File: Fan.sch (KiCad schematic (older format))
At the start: 0 parts

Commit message: Added Powercontrol stuff
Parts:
- added Q?: MOSFET_N, ~, symbol MOSFET_N
- added R? (x5): R, ~, symbol R
- added RV?: POT, ~, symbol POT
- added U?: LM324, symbol LM324
- added U?: MCP4922-E/P, DIP14, symbol MCP4922-E/P
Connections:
- net labels added: +12V, -12V, AGND, CS_N, Current Measure, Fan_in, MISO, MOSI, SCLK, Tach_out
- net labels removed: Fanin, Tachout
- wire segments 0 -> 34

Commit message: Struktur nach Arduino
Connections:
- net labels added: CURR_MEAS, FAN_EN_N, FAN_OUT+, FAN_OUT-, TACH_IN, TACH_MEAS
- net labels removed: Current Measure, Fan_in, Power+, Power-, Tach, Tach_out
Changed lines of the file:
@@
 Sheet 8 9
 Title ""
-Date "4 feb 2014"
+Date "6 feb 2014"
 Rev ""
 Comp ""
@@
 Comment4 ""
 $EndDescr
-Text HLabel 10500 2200 0    60   Input ~ 0
-Power+
-Text HLabel 10500 2400 0    60   Input ~ 0
-Power-
+Text HLabel 10500 2200 0    60   Output ~ 0
+FAN_OUT+
+Text HLabel 10500 2400 0    60   Output ~ 0
+FAN_OUT-
 Text HLabel 10350 2800 0    60   Input ~ 0
-Tach
+TACH_IN
 Text HLabel 1350 3300 0    60   Output ~ 0
-Tach_out
+TACH_MEAS
 Text HLabel 1350 2700 0    60   Input ~ 0
-Fan_in
+FAN_EN_N
 $Comp
 L LM324 U?
@@
 $EndComp
 Text HLabel 1400 2900 0    60   Output ~ 0
-Current Measure
+CURR_MEAS
 $Comp
 L R R?

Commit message: Fan/Current Module Refactoring
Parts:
- removed R? (x3): R, ~, symbol R
- removed RV?: POT, ~, symbol POT
- added D?: DIODE, ~, symbol DIODE
- added Q? (x2): MOSFET_N, ~, symbol MOSFET_N
- added TH?: THERMISTOR, ~, symbol THERMISTOR
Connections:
- net labels added: +12C, FAN_MODE, FAN_PWM_N
- net labels removed: FAN_EN_N
- wire segments 34 -> 36
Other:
- moved on the sheet: Q?, R?, U?, U?A

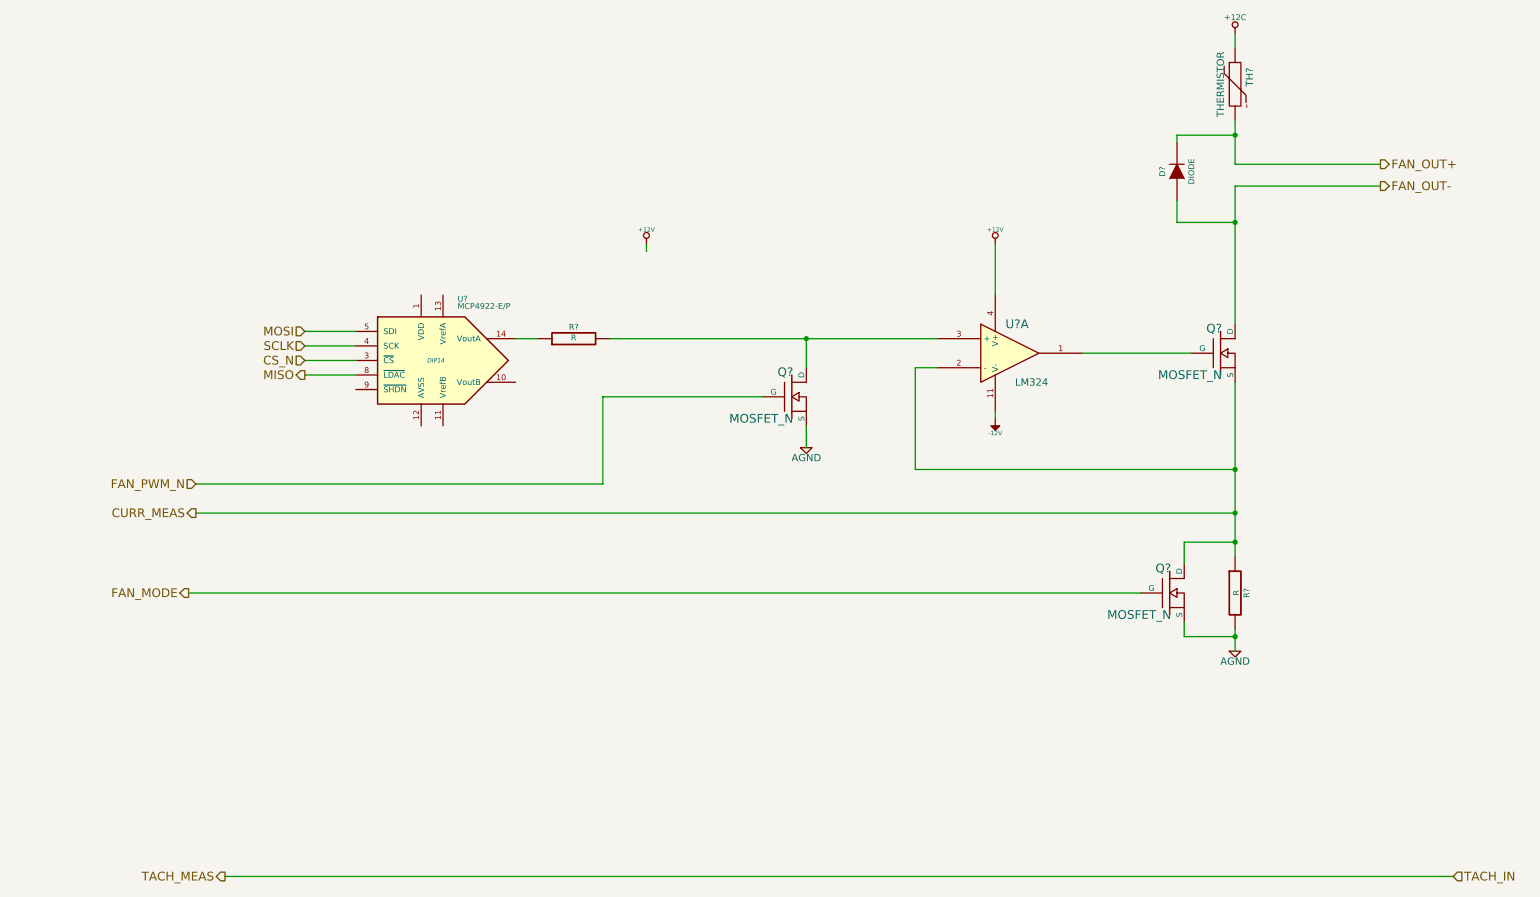
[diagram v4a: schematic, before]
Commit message: Nach Einfuegen Relay-Modul
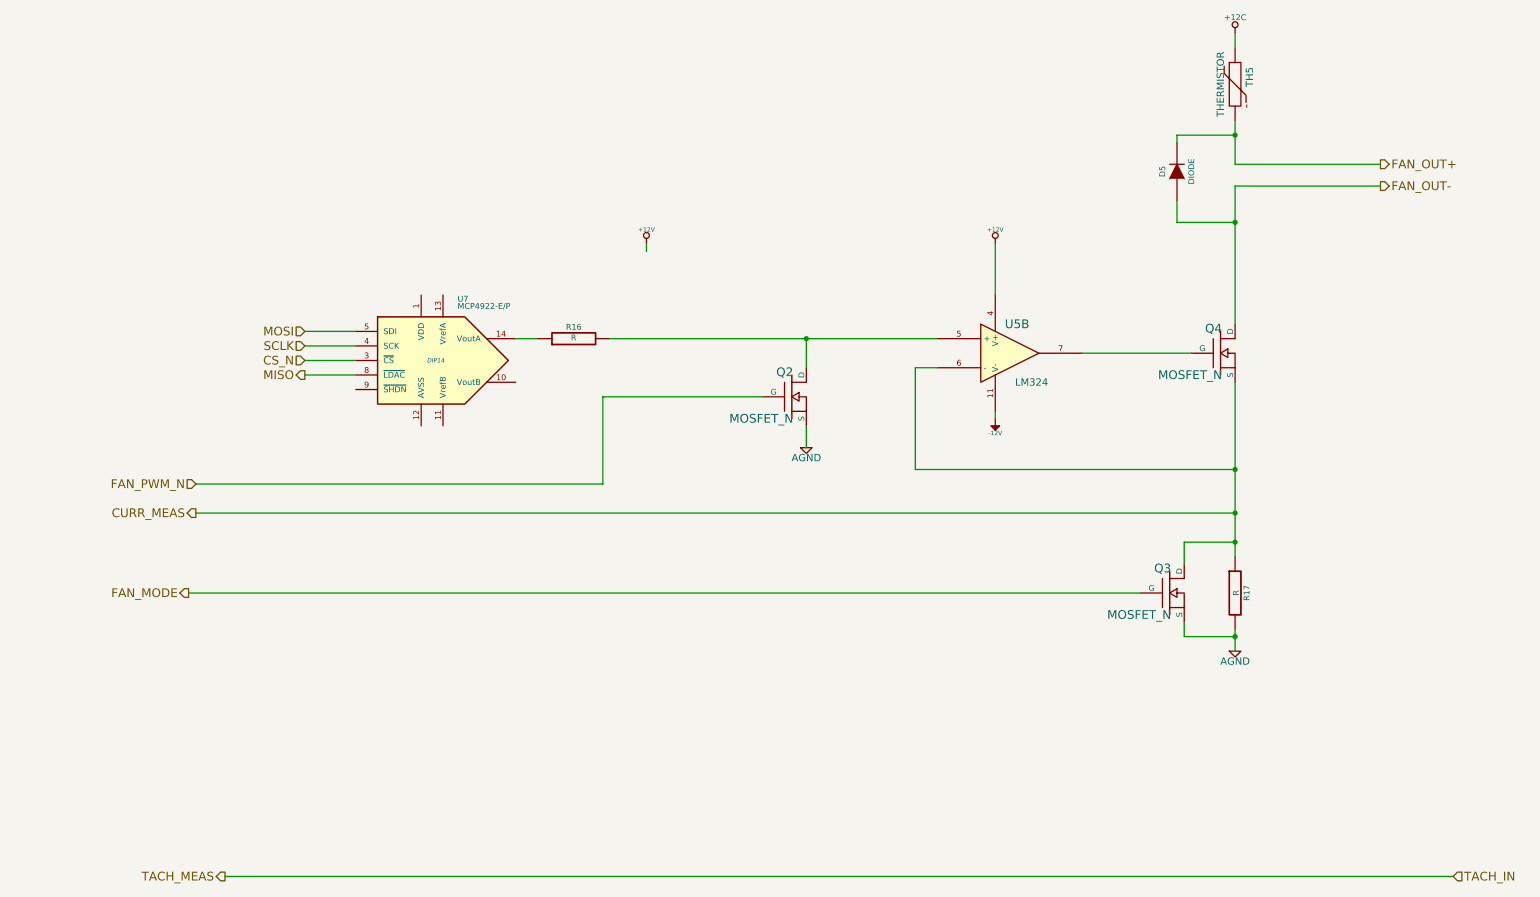
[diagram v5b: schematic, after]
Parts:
- gave numbers to parts that had none: 9
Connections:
- net CURR_MEAS: now also U5.6 (-); no longer U5.2 (-)
- net at Q4.1 (G): now also U5.7; no longer U5.1
- net at Q2.2 (D), R16.2: now also U5.5 (+); no longer U5.3 (+)
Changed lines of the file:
@@
 Sheet 7 9
 Title ""
-Date "14 feb 2014"
+Date "17 feb 2014"
 Rev ""
 Comp ""
@@
 FAN_PWM_N
 $Comp
-L LM324 U?
-U 1 1 52F0A102
+L LM324 U5
+U 2 1 52F0A102
 P 7300 2900
-F 0 "U?" H 7350 3100 60  0000 C CNN
+F 0 "U5" H 7350 3100 60  0000 C CNN
 F 1 "LM324" H 7450 2700 50  0000 C CNN
 F 2 "" H 7300 2900 60  0000 C CNN
 F 3 "" H 7300 2900 60  0000 C CNN
-	1    7300 2900
-	1    0    0    -1
-$EndComp
-$Comp
-L MOSFET_N Q?
+	2    7300 2900
+	1    0    0    -1
+$EndComp
+$Comp
+L MOSFET_N Q4
 U 1 1 52F0A120
 P 8750 2900
-F 0 "Q?" H 8760 3070 60  0000 R CNN
+F 0 "Q4" H 8760 3070 60  0000 R CNN
 F 1 "MOSFET_N" H 8760 2750 60  0000 R CNN
 F 2 "~" H 8750 2900 60  0000 C CNN
@@
 $EndComp
 $Comp
-L R R?
+L R R17
 U 1 1 52F0A144
 P 8850 4550
-F 0 "R?" V 8930 4550 40  0000 C CNN
+F 0 "R17" V 8930 4550 40  0000 C CNN
 F 1 "R" V 8857 4551 40  0000 C CNN
 F 2 "~" V 8780 4550 30  0000 C CNN
@@
 $EndComp
 $Comp
-L AGND #PWR?
+L AGND #PWR41
 U 1 1 52F0A153
 P 8850 4950
-F 0 "#PWR?" H 8850 4950 40  0001 C CNN
+F 0 "#PWR41" H 8850 4950 40  0001 C CNN
 F 1 "AGND" H 8850 4880 50  0000 C CNN
 F 2 "" H 8850 4950 60  0000 C CNN
@@
 $EndComp
 $Comp
-L +12V #PWR?
+L +12V #PWR38
 U 1 1 52F0A1B1
 P 7200 2150
-F 0 "#PWR?" H 7200 2100 20  0001 C CNN
+F 0 "#PWR38" H 7200 2100 20  0001 C CNN
 F 1 "+12V" H 7200 2250 30  0000 C CNN
 F 2 "" H 7200 2150 60  0000 C CNN
@@
 $EndComp
 $Comp
-L -12V #PWR?
+L -12V #PWR39
 U 1 1 52F0A1E4
 P 7200 3350
-F 0 "#PWR?" H 7200 3480 20  0001 C CNN
+F 0 "#PWR39" H 7200 3480 20  0001 C CNN
 F 1 "-12V" H 7200 3450 30  0000 C CNN
 F 2 "" H 7200 3350 60  0000 C CNN
@@
 $EndComp
 $Comp
-L +12V #PWR?
+L +12V #PWR36
 U 1 1 52F0A28E
 P 4800 2150
-F 0 "#PWR?" H 4800 2100 20  0001 C CNN
+F 0 "#PWR36" H 4800 2100 20  0001 C CNN
 F 1 "+12V" H 4800 2250 30  0000 C CNN
 F 2 "" H 4800 2150 60  0000 C CNN
@@
 $EndComp
 $Comp
-L AGND #PWR?
+L AGND #PWR37
 U 1 1 52F0A2CD
 P 5900 3550
-F 0 "#PWR?" H 5900 3550 40  0001 C CNN
+F 0 "#PWR37" H 5900 3550 40  0001 C CNN
 F 1 "AGND" H 5900 3480 50  0000 C CNN
 F 2 "" H 5900 3550 60  0000 C CNN
@@
 $EndComp
 $Comp
-L MCP4922-E/P U?
+L MCP4922-E/P U7
 U 1 1 52F0A360
 P 3350 2950
-F 0 "U?" H 3500 3350 40  0000 L BNN
+F 0 "U7" H 3500 3350 40  0000 L BNN
 F 1 "MCP4922-E/P" H 3500 3300 40  0000 L BNN
 F 2 "DIP14" H 3350 2950 30  0000 C CIN
@@
 CURR_MEAS
 $Comp
-L R R?
+L R R16
 U 1 1 52F0A4D1
 P 4300 2800
-F 0 "R?" V 4380 2800 40  0000 C CNN
+F 0 "R16" V 4380 2800 40  0000 C CNN
 F 1 "R" V 4307 2801 40  0000 C CNN
 F 2 "~" V 4230 2800 30  0000 C CNN
@@
 	2800 3050 2450 3050
 $Comp
-L MOSFET_N Q?
+L MOSFET_N Q3
 U 1 1 52F3A8AB
 P 8400 4550
-F 0 "Q?" H 8410 4720 60  0000 R CNN
+F 0 "Q3" H 8410 4720 60  0000 R CNN
 F 1 "MOSFET_N" H 8410 4400 60  0000 R CNN
 F 2 "~" H 8400 4550 60  0000 C CNN
@@
 $EndComp
 $Comp
-L THERMISTOR TH?
+L THERMISTOR TH5
 U 1 1 52F3A947
 P 8850 1050
-F 0 "TH?" V 8950 1100 50  0000 C CNN
+F 0 "TH5" V 8950 1100 50  0000 C CNN
 F 1 "THERMISTOR" V 8750 1050 50  0000 C CNN
 F 2 "~" H 8850 1050 60  0000 C CNN
@@
 	8850 1300 8850 1600
 $Comp
-L DIODE D?
+L DIODE D5
 U 1 1 52F3AA39
 P 8450 1650
-F 0 "D?" H 8450 1750 40  0000 C CNN
+F 0 "D5" H 8450 1750 40  0000 C CNN
 F 1 "DIODE" H 8450 1550 40  0000 C CNN
 F 2 "~" H 8450 1650 60  0000 C CNN
@@
 	6800 2800 4550 2800
 $Comp
-L MOSFET_N Q?
+L MOSFET_N Q2
 U 1 1 52F3AD13
 P 5800 3200
-F 0 "Q?" H 5810 3370 60  0000 R CNN
+F 0 "Q2" H 5810 3370 60  0000 R CNN
 F 1 "MOSFET_N" H 5810 3050 60  0000 R CNN
 F 2 "~" H 5800 3200 60  0000 C CNN
@@
 Connection ~ 5900 2800
 $Comp
-L +12C #PWR?
+L +12C #PWR40
 U 1 1 52F3B1FC
 P 8850 700
-F 0 "#PWR?" H 8850 670 30  0001 C CNN
+F 0 "#PWR40" H 8850 670 30  0001 C CNN
 F 1 "+12C" H 8850 810 40  0000 C CNN
 F 2 "" H 8850 700 60  0000 C CNN

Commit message: Am Ende der 5. Woche.
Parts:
- removed Q3, Q4: MOSFET_N, ~, symbol MOSFET_N
- removed U7: MCP4922-E/P, DIP14, symbol MCP4922-E/P
- added C12, C13: C, ~, symbol C
- added Q3, Q4: AOD476, ~, symbol MOS_N_NUM
- added U5: MCP4801, symbol MCP4801
- D5: value DIODE -> B130-13-F; MFG Name (none) -> Diodes Inc; MFG Part Number (none) -> B130-13-F
- Q2: value MOSFET_N -> DMN65D8L-7; MFG Name (none) -> Diodes Inc; MFG Part Number (none) -> DMN65D8L-7
- TH5: value THERMISTOR -> MINISMDC050F-2; MFG Name (none) -> TE Connectivity; MFG Part Number (none) -> MINISMDC050F-2
- U4: renamed from U5; value LM324 -> OPA4170
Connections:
- net labels added: +5V, ~LDAC, ~SHDN
- net labels removed: MISO
- wire segments 36 -> 45
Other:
- note added: "Should this be a different ground?"
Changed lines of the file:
@@
 Sheet 7 9
 Title ""
-Date "17 feb 2014"
+Date "22 feb 2014"
 Rev ""
 Comp ""
@@
 FAN_PWM_N
 $Comp
-L LM324 U5
+L LM324 U4
 U 2 1 52F0A102
 P 7300 2900
-F 0 "U5" H 7350 3100 60  0000 C CNN
-F 1 "LM324" H 7450 2700 50  0000 C CNN
+F 0 "U4" H 7350 3100 60  0000 C CNN
+F 1 "OPA4170" H 7450 2700 50  0000 C CNN
 F 2 "" H 7300 2900 60  0000 C CNN
 F 3 "" H 7300 2900 60  0000 C CNN
 	2    7300 2900
-	1    0    0    -1
-$EndComp
-$Comp
-L MOSFET_N Q4
-U 1 1 52F0A120
-P 8750 2900
-F 0 "Q4" H 8760 3070 60  0000 R CNN
-F 1 "MOSFET_N" H 8760 2750 60  0000 R CNN
-F 2 "~" H 8750 2900 60  0000 C CNN
-F 3 "~" H 8750 2900 60  0000 C CNN
-	1    8750 2900
 	1    0    0    -1
 $EndComp
@@
 $EndComp
 $Comp
-L AGND #PWR41
+L AGND #PWR041
 U 1 1 52F0A153
 P 8850 4950
-F 0 "#PWR41" H 8850 4950 40  0001 C CNN
+F 0 "#PWR041" H 8850 4950 40  0001 C CNN
 F 1 "AGND" H 8850 4880 50  0000 C CNN
 F 2 "" H 8850 4950 60  0000 C CNN
@@
 $EndComp
 $Comp
-L +12V #PWR38
+L +12V #PWR042
 U 1 1 52F0A1B1
 P 7200 2150
-F 0 "#PWR38" H 7200 2100 20  0001 C CNN
+F 0 "#PWR042" H 7200 2100 20  0001 C CNN
 F 1 "+12V" H 7200 2250 30  0000 C CNN
 F 2 "" H 7200 2150 60  0000 C CNN
@@
 $EndComp
 $Comp
-L -12V #PWR39
+L -12V #PWR043
 U 1 1 52F0A1E4
 P 7200 3350
-F 0 "#PWR39" H 7200 3480 20  0001 C CNN
+F 0 "#PWR043" H 7200 3480 20  0001 C CNN
 F 1 "-12V" H 7200 3450 30  0000 C CNN
 F 2 "" H 7200 3350 60  0000 C CNN
@@
 $EndComp
 $Comp
-L +12V #PWR36
-U 1 1 52F0A28E
-P 4800 2150
-F 0 "#PWR36" H 4800 2100 20  0001 C CNN
-F 1 "+12V" H 4800 2250 30  0000 C CNN
-F 2 "" H 4800 2150 60  0000 C CNN
-F 3 "" H 4800 2150 60  0000 C CNN
-	1    4800 2150
-	1    0    0    -1
-$EndComp
-$Comp
-L AGND #PWR37
+L AGND #PWR044
 U 1 1 52F0A2CD
 P 5900 3550
-F 0 "#PWR37" H 5900 3550 40  0001 C CNN
+F 0 "#PWR044" H 5900 3550 40  0001 C CNN
 F 1 "AGND" H 5900 3480 50  0000 C CNN
 F 2 "" H 5900 3550 60  0000 C CNN
 F 3 "" H 5900 3550 60  0000 C CNN
 	1    5900 3550
-	1    0    0    -1
-$EndComp
-$Comp
-L MCP4922-E/P U7
-U 1 1 52F0A360
-P 3350 2950
-F 0 "U7" H 3500 3350 40  0000 L BNN
-F 1 "MCP4922-E/P" H 3500 3300 40  0000 L BNN
-F 2 "DIP14" H 3350 2950 30  0000 C CIN
-F 3 "" H 3350 2950 60  0000 C CNN
-	1    3350 2950
 	1    0    0    -1
 $EndComp
@@
 	7200 2150 7200 2500
 Wire Wire Line
-	4800 2200 4800 2150
-Wire Wire Line
 	1700 4000 8850 4000
-Wire Wire Line
-	4050 2800 3900 2800
-Text HLabel 2450 2750 0    60   Input ~ 0
+Text HLabel 2100 2800 0    60   Input ~ 0
 MOSI
-Text HLabel 2450 3050 0    60   Output ~ 0
-MISO
-Text HLabel 2450 2950 0    60   Input ~ 0
+Text HLabel 2100 2500 0    60   Input ~ 0
 CS_N
-Text HLabel 2450 2850 0    60   Input ~ 0
+Text HLabel 2100 2650 0    60   Input ~ 0
 SCLK
 Wire Wire Line
-	2800 2750 2450 2750
-Wire Wire Line
-	2800 2850 2450 2850
-Wire Wire Line
 	2800 2950 2450 2950
-Wire Wire Line
-	2800 3050 2450 3050
-$Comp
-L MOSFET_N Q3
-U 1 1 52F3A8AB
-P 8400 4550
-F 0 "Q3" H 8410 4720 60  0000 R CNN
-F 1 "MOSFET_N" H 8410 4400 60  0000 R CNN
-F 2 "~" H 8400 4550 60  0000 C CNN
-F 3 "~" H 8400 4550 60  0000 C CNN
-	1    8400 4550
-	1    0    0    -1
-$EndComp
 $Comp
 L THERMISTOR TH5
@@
 P 8850 1050
 F 0 "TH5" V 8950 1100 50  0000 C CNN
-F 1 "THERMISTOR" V 8750 1050 50  0000 C CNN
+F 1 "MINISMDC050F-2" V 8750 1050 50  0000 C CNN
 F 2 "~" H 8850 1050 60  0000 C CNN
 F 3 "~" H 8850 1050 60  0000 C CNN
+F 4 "TE Connectivity" H 8850 1050 60  0001 C CNN "MFG Name"
+F 5 "MINISMDC050F-2" H 8850 1050 60  0001 C CNN "MFG Part Number"
 	1    8850 1050
 	1    0    0    -1
@@
 P 8450 1650
 F 0 "D5" H 8450 1750 40  0000 C CNN
-F 1 "DIODE" H 8450 1550 40  0000 C CNN
+F 1 "B130-13-F" H 8450 1550 40  0000 C CNN
 F 2 "~" H 8450 1650 60  0000 C CNN
 F 3 "~" H 8450 1650 60  0000 C CNN
+F 4 "Diodes Inc" H 8450 1650 60  0001 C CNN "MFG Name"
+F 5 "B130-13-F" H 8450 1650 60  0001 C CNN "MFG Part Number"
 	1    8450 1650
 	0    -1   -1   0
@@
 P 5800 3200
 F 0 "Q2" H 5810 3370 60  0000 R CNN
-F 1 "MOSFET_N" H 5810 3050 60  0000 R CNN
+F 1 "DMN65D8L-7" H 5810 3050 60  0000 R CNN
 F 2 "~" H 5800 3200 60  0000 C CNN
 F 3 "~" H 5800 3200 60  0000 C CNN
+F 4 "Diodes Inc" H 5800 3200 60  0001 C CNN "MFG Name"
+F 5 "DMN65D8L-7" H 5800 3200 60  0001 C CNN "MFG Part Number"
 	1    5800 3200
 	1    0    0    -1
@@
 Connection ~ 5900 2800
 $Comp
-L +12C #PWR40
+L +12C #PWR045
 U 1 1 52F3B1FC
 P 8850 700
-F 0 "#PWR40" H 8850 670 30  0001 C CNN
+F 0 "#PWR045" H 8850 670 30  0001 C CNN
 F 1 "+12C" H 8850 810 40  0000 C CNN
 F 2 "" H 8850 700 60  0000 C CNN
@@
 	1    0    0    -1
 $EndComp
+$Comp
+L MCP4801 U5
+U 1 1 5305D736
+P 3000 2800
+F 0 "U5" H 3100 2300 60  0000 C CNN
+F 1 "MCP4801" H 3150 2900 60  0000 C CNN
+F 2 "" H 3450 2300 60  0000 C CNN
+F 3 "" H 3450 2300 60  0000 C CNN
+	1    3000 2800
+	1    0    0    -1
+$EndComp
+Wire Wire Line
+	4050 2800 3850 2800
+Wire Wire Line
+	2350 2500 2100 2500
+Wire Wire Line
+	2350 2650 2100 2650
+Wire Wire Line
+	2350 2800 2100 2800
+Text HLabel 2100 2950 0    60   Input ~ 0
+~LDAC
+Text HLabel 2100 3100 0    60   Input ~ 0
+~SHDN
+Wire Wire Line
+	2350 2950 2100 2950
+Wire Wire Line
+	2350 3100 2100 3100
+$Comp
+L +5V #PWR046
+U 1 1 530700A7
+P 3000 1750
+F 0 "#PWR046" H 3000 1840 20  0001 C CNN
+F 1 "+5V" H 3000 1840 30  0000 C CNN
+F 2 "" H 3000 1750 60  0000 C CNN
+F 3 "" H 3000 1750 60  0000 C CNN
+	1    3000 1750
+	1    0    0    -1
+$EndComp
+Wire Wire Line
+	3000 2050 3000 1750
+$Comp
+L C C12
+U 1 1 530700EE
+P 2700 1900
+F 0 "C12" H 2700 2000 40  0000 L CNN
+F 1 "C" H 2706 1815 40  0000 L CNN
+F 2 "~" H 2738 1750 30  0000 C CNN
+F 3 "~" H 2700 1900 60  0000 C CNN
+	1    2700 1900
+	0    -1   -1   0
+$EndComp
+Wire Wire Line
+	3000 1900 2900 1900
+Connection ~ 3000 1900
+Wire Wire Line
+	2500 1900 2300 1900
+Wire Wire Line
+	2300 1900 2300 2150
+$Comp
+L AGND #PWR047
+U 1 1 5307019E
+P 3000 3600
+F 0 "#PWR047" H 3000 3600 40  0001 C CNN
+F 1 "AGND" H 3000 3530 50  0000 C CNN
+F 2 "" H 3000 3600 60  0000 C CNN
+F 3 "" H 3000 3600 60  0000 C CNN
+	1    3000 3600
+	1    0    0    -1
+$EndComp
+$Comp
+L AGND #PWR048
+U 1 1 530701A4
+P 2300 2150
+F 0 "#PWR048" H 2300 2150 40  0001 C CNN
+F 1 "AGND" H 2300 2080 50  0000 C CNN
+F 2 "" H 2300 2150 60  0000 C CNN
+F 3 "" H 2300 2150 60  0000 C CNN
+	1    2300 2150
+	1    0    0    -1
+$EndComp
+Wire Wire Line
+	3000 3550 3000 3600
+$Comp
+L C C13
+U 1 1 530705E5
+P 9250 750
+F 0 "C13" H 9250 850 40  0000 L CNN
+F 1 "C" H 9256 665 40  0000 L CNN
+F 2 "~" H 9288 600 30  0000 C CNN
+F 3 "~" H 9250 750 60  0000 C CNN
+	1    9250 750
+	0    -1   -1   0
+$EndComp
+$Comp
+L AGND #PWR049
+U 1 1 530705ED
+P 9550 900
+F 0 "#PWR049" H 9550 900 40  0001 C CNN
+F 1 "AGND" H 9550 830 50  0000 C CNN
+F 2 "" H 9550 900 60  0000 C CNN
+F 3 "" H 9550 900 60  0000 C CNN
+	1    9550 900
+	1    0    0    -1
+$EndComp
+Wire Wire Line
+	9050 750  8850 750
+Connection ~ 8850 750
+Wire Wire Line
+	9450 750  9550 750
+Wire Wire Line
+	9550 750  9550 900
+Text Notes 10650 1150 2    60   ~ 0
+Should this be a different ground?
+Text Notes 10100 5400 2    60   ~ 0
+Should this be a different ground?
+$Comp
+L MOS_N_NUM Q4
+U 1 1 530627C9
+P 8750 2900
+F 0 "Q4" H 8760 3070 60  0000 R CNN
+F 1 "AOD476" H 8760 2750 60  0000 R CNN
+F 2 "~" H 8750 2900 60  0000 C CNN
+F 3 "~" H 8750 2900 60  0000 C CNN
+F 4 "Alpha and Omega" H 8750 2900 60  0001 C CNN "MFG Name"
+F 5 "AOD476" H 8750 2900 60  0001 C CNN "MFG Part Number"
+	1    8750 2900
+	1    0    0    -1
+$EndComp
+$Comp
+L MOS_N_NUM Q3
+U 1 1 5306282C
+P 8400 4550
+F 0 "Q3" H 8410 4720 60  0000 R CNN
+F 1 "AOD476" H 8410 4400 60  0000 R CNN
+F 2 "~" H 8400 4550 60  0000 C CNN
+F 3 "~" H 8400 4550 60  0000 C CNN
+F 4 "Alpha and Omega" H 8400 4550 60  0001 C CNN "MFG Name"
+F 5 "AOD476" H 8400 4550 60  0001 C CNN "MFG Part Number"
+	1    8400 4550
+	1    0    0    -1
+$EndComp
